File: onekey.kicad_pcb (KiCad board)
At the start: 2 copper layers, 18.4 x 24.8 mm, 12 parts, among them SW1 SPST, U1 ATMEGA32U4-M, U2 USB_TYPE_C, X1 XTAL

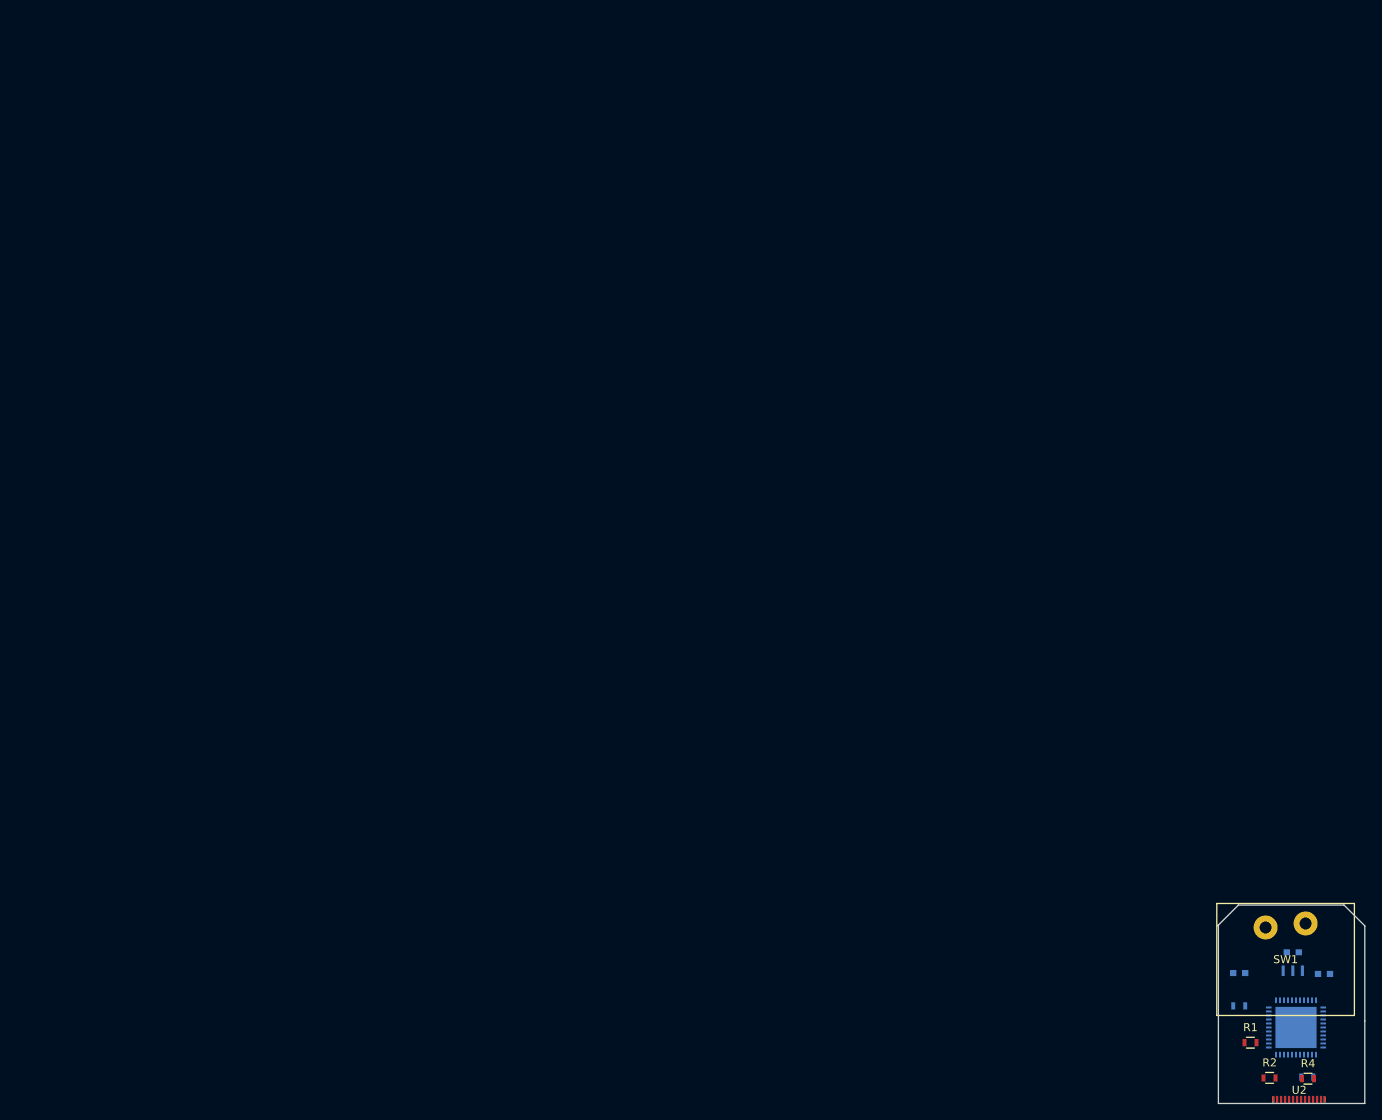
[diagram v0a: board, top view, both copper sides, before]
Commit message: add mounting hole for standoff
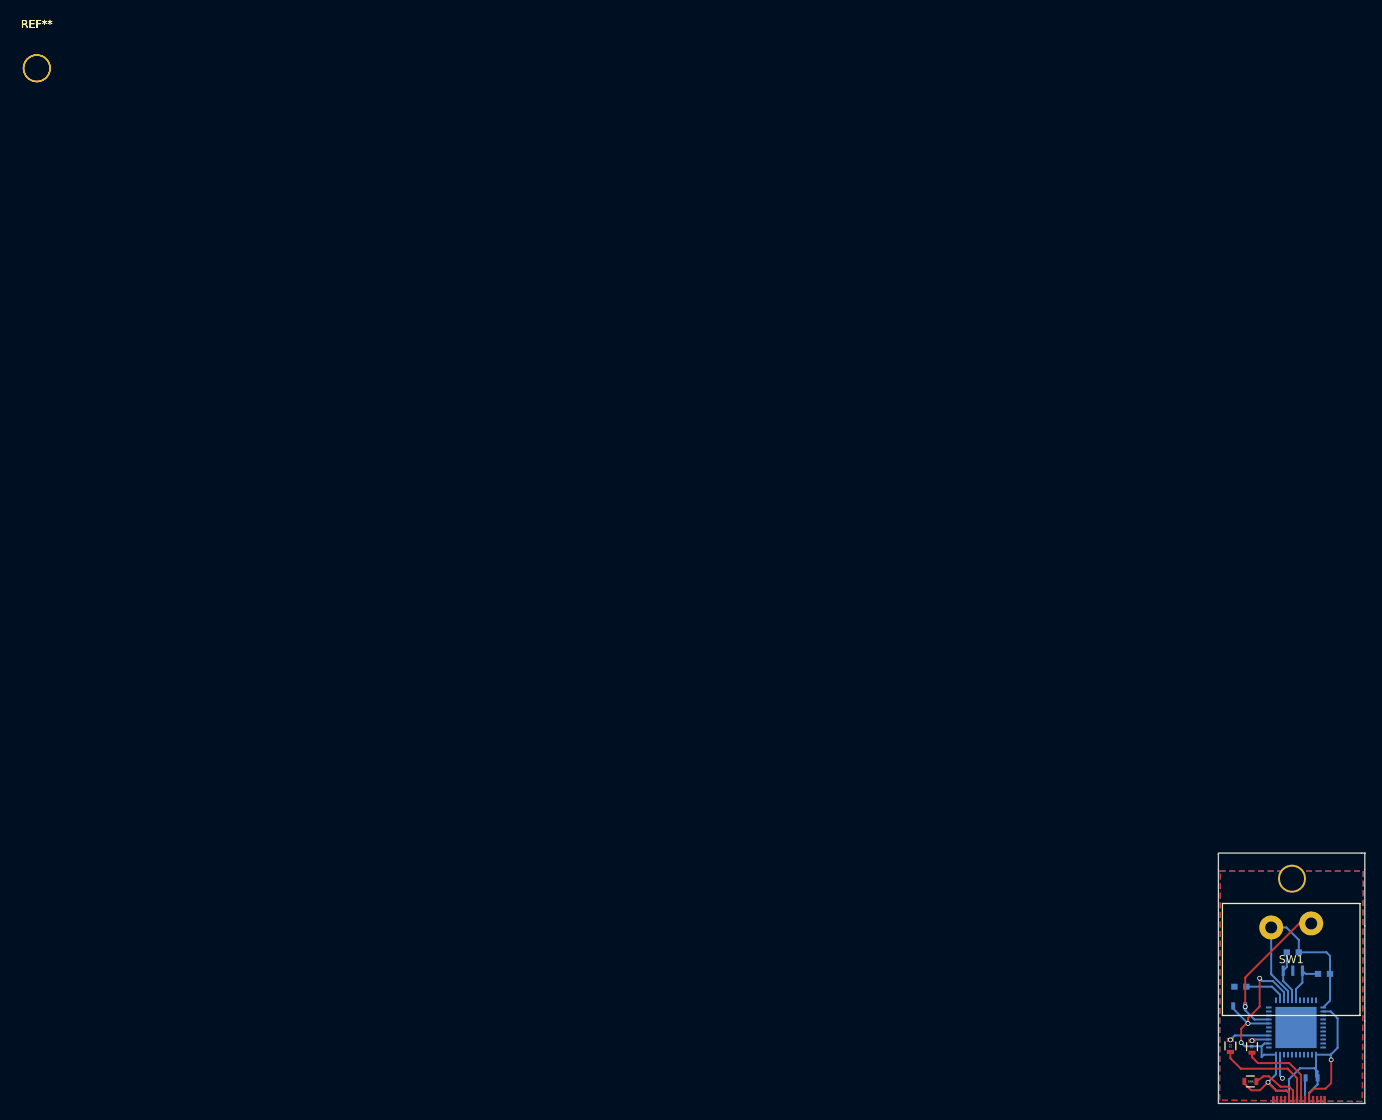
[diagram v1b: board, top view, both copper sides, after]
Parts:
- added REF** (x2): MountingHole_3mm, Mounting_Holes:MountingHole_4mm, F.Cu at (0.00, 0.00)
- added REF**: MountingHole_3mm, Mounting_Holes:MountingHole3mm, F.Cu at (156.9, 101.3)
- moved R4 7.21 mm to (151.7, 126.7), turned to 180 degrees
- moved R2 4.48 mm to (151.9, 122.3), turned to 270 degrees
- moved R1 2.53 mm to (149.2, 122.2), turned to 270 degrees
- moved W1 1.71 mm to (150.4, 114.8)
- moved SW1 0.70 mm to (154.3, 107.4)
- moved R5 0.56 mm to (159.3, 126.2)
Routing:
- net /VCC: track 0.00 -> 72.8 mm, vias 0 -> 5
- net GND: track 0.00 -> 29.9 mm, vias 0 -> 1
- net Net-(R3-Pad1): track 0.00 -> 18.8 mm, vias 0 -> 1
- net /D+: track 0.00 -> 12.9 mm
- net /D-: track 0.00 -> 10.7 mm
- net Net-(C2-Pad2): track 0.00 -> 6.64 mm
- net Net-(R4-Pad1): track 0.00 -> 6.61 mm
- net Net-(C1-Pad2): track 0.00 -> 6.15 mm
- net Net-(U1-Pad13): track 0.00 -> 5.31 mm
- net Net-(R1-Pad1): track 0.00 -> 5.03 mm, vias 0 -> 1
- net Net-(R5-Pad1): track 0.00 -> 2.75 mm
- net Net-(R2-Pad1): track 0.00 -> 2.16 mm, vias 0 -> 1
- added copper zone on B.Cu, net GND
- added copper zone on F.Cu, net GND
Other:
- board size 18.4 x 24.8 mm -> 18.4 x 31.3 mm
